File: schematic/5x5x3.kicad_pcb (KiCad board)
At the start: 4 copper layers, 100 x 100 mm, 137 parts, among them J1 SW Debug, J11 Conn_01x03_Male, J12 Conn_01x03_Male, J3 Conn_01x03_Male, J4 Conn_01x03_Male, J7 Conn_01x03_Male, SW11 SW, SW12 SW, SW13 SW, SW14 SW, SW21 SW, SW22 SW, SW23 SW, SW24 SW, SW25 SW, SW31 SW, SW32 SW, SW33 SW, SW34 SW, SW35 SW, SW41 SW, SW42 SW, SW43 SW, SW44 SW, SW45 SW, SW51 SW, SW52 SW, SW53 SW, SW54 SW, SW55 SW, SW6 ALPS_EC11, U1 nice_nano v2

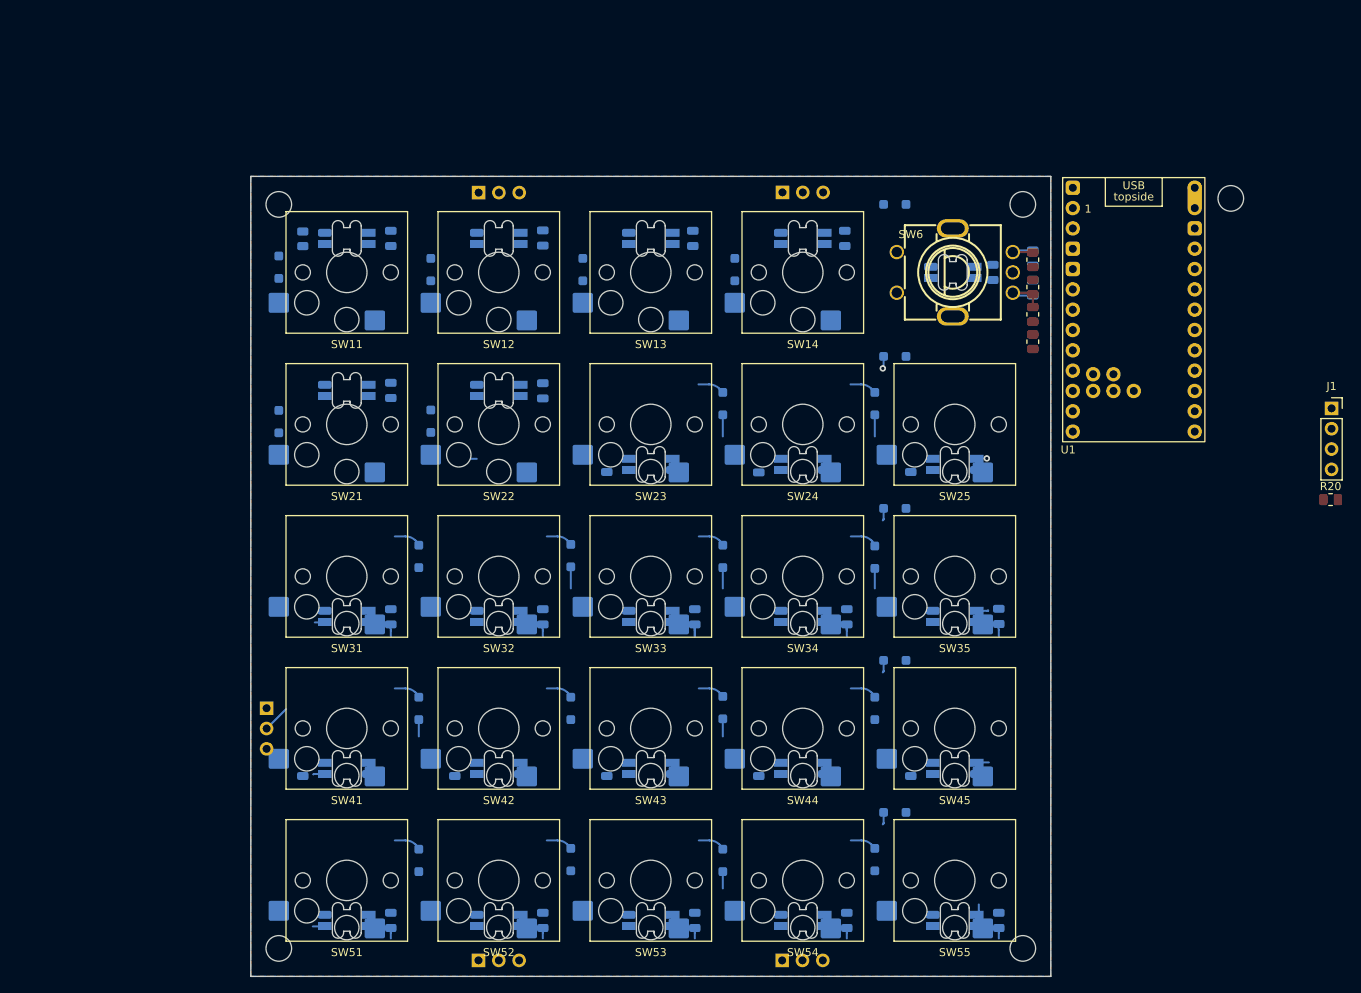
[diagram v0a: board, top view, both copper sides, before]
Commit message: Connect up the keys, rough placing of components
Need to find a good switch, and maybe rearrange the row / col pins to
better align with 5x5 layout.

Currently targetting 4 layer board
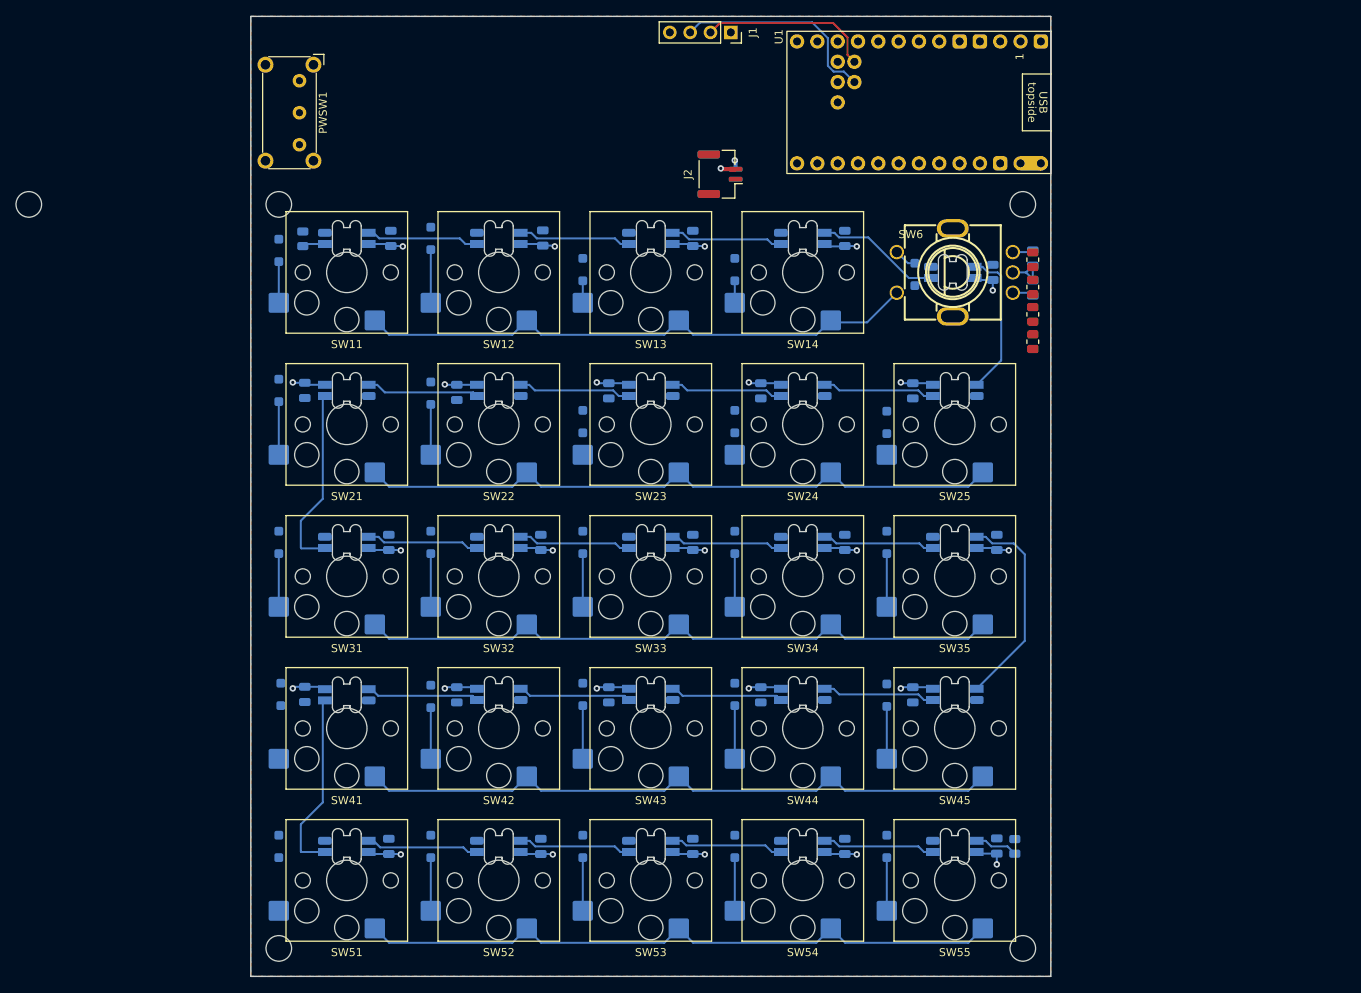
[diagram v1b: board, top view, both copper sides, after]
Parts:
- removed J11, J12, J4, J7: Conn_01x03_Male, Connector_PinSocket_2.54mm:PinSocket_1x03_P2.54mm_Vertical
- removed kibuzzard-62AF6B0E: G***, kibuzzard-62AF6B0E
- removed kibuzzard-62AF6B38: G***, kibuzzard-62AF6B38
- removed kibuzzard-62AF6B7C: G***, kibuzzard-62AF6B7C
- removed kibuzzard-62AF6BA3: G***, kibuzzard-62AF6BA3
- removed kibuzzard-62AF6BAD: G***, kibuzzard-62AF6BAD
- removed kibuzzard-62AF6BF3: G***, kibuzzard-62AF6BF3
- removed kibuzzard-62AF6D1E (x2): G***, kibuzzard-62AF6D1E
- removed kibuzzard-62AF6DB1 (x2): G***, kibuzzard-62AF6DB1
- removed kibuzzard-62AF6E15: G***, kibuzzard-62AF6E15
- removed kibuzzard-62AF6E21: G***, kibuzzard-62AF6E21
- removed kibuzzard-62AF6EB6: G***, kibuzzard-62AF6EB6
- removed kibuzzard-62AF6EDD: G***, kibuzzard-62AF6EDD
- removed kibuzzard-62AF6F00: G***, kibuzzard-62AF6F00
- removed kibuzzard-62AF6F11: G***, kibuzzard-62AF6F11
- added J2: Battery, Connector_JST:JST_GH_BM02B-GHS-TBT_1x02-1MP_P1.25mm_Vertical, F.Cu at (94.7, 37.7)
- added PWSW1: SW_SPST, Button_Switch_THT:SW_E-Switch_EG1224_SPDT_Angled, F.Cu at (42.1, 26.0)
- J3: value Conn_01x03_Male -> Battery; footprint Connector_PinSocket_2.54mm:PinSocket_1x03_P2.54mm_Vertical -> Connector_JST:JST_GH_BM02B-GHS-TBT_1x02-1MP_P1.25mm_Vertical
- R20: moved to B.Cu
- moved ? 150.3 mm to (8.25, 41.5)
- moved J1 88.6 mm to (96.0, 20.0), turned to -90 degrees
- moved R20 58.6 mm to (131.5, 121.8), turned to 90 degrees
- moved U1 39.1 mm to (118.2, 28.8), turned to -90 degrees
- moved J3 30.3 mm to (94.7, 37.7)
- moved D23 17.6 mm to (77.5, 68.7), turned to -90 degrees
- moved D24 17.6 mm to (96.5, 68.7), turned to -90 degrees
- moved D34 17.6 mm to (96.5, 83.8), turned to -90 degrees
- moved D31 17.6 mm to (39.5, 83.8), turned to -90 degrees
- moved D33 17.6 mm to (77.5, 83.8), turned to -90 degrees
- moved D44 17.6 mm to (96.5, 102.8), turned to -90 degrees
- moved D51 17.6 mm to (39.5, 121.8), turned to -90 degrees
- moved D53 17.6 mm to (77.5, 121.8), turned to -90 degrees
- moved D32 17.6 mm to (58.5, 83.8), turned to -90 degrees
- moved D43 17.6 mm to (77.5, 102.8), turned to -90 degrees
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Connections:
- C11 pad 1: Vusb -> Vext
- C12 pad 1: Vusb -> Vext
- C13 pad 1: Vusb -> Vext
- C14 pad 1: Vusb -> Vext
- C15 pad 1: Vusb -> Vext
- C21 pad 1: Vusb -> Vext
- C22 pad 1: Vusb -> Vext
- C23 pad 1: Vusb -> Vext
- C24 pad 1: Vusb -> Vext
- C25 pad 1: Vusb -> Vext
- C31 pad 1: Vusb -> Vext
- C32 pad 1: Vusb -> Vext
- C33 pad 1: Vusb -> Vext
- C34 pad 1: Vusb -> Vext
- C35 pad 1: Vusb -> Vext
- C41 pad 1: Vusb -> Vext
- C42 pad 1: Vusb -> Vext
- C43 pad 1: Vusb -> Vext
- C44 pad 1: Vusb -> Vext
- C45 pad 1: Vusb -> Vext
- C51 pad 1: Vusb -> Vext
- C52 pad 1: Vusb -> Vext
- C53 pad 1: Vusb -> Vext
- C54 pad 1: Vusb -> Vext
- C55 pad 1: Vusb -> Vext
- J1 pad 1: +3V3 -> Vbatt
- J3 pad 1: GND -> Vbatt
- LED11 pad 1: Vusb -> Vext
- LED12 pad 1: Vusb -> Vext
- LED13 pad 1: Vusb -> Vext
- LED14 pad 1: Vusb -> Vext
- LED15 pad 1: Vusb -> Vext
- LED21 pad 1: Vusb -> Vext
- LED22 pad 1: Vusb -> Vext
- LED23 pad 1: Vusb -> Vext
- LED24 pad 1: Vusb -> Vext
- LED25 pad 1: Vusb -> Vext
- LED31 pad 1: Vusb -> Vext
- LED32 pad 1: Vusb -> Vext
- LED33 pad 1: Vusb -> Vext
- LED34 pad 1: Vusb -> Vext
- LED35 pad 1: Vusb -> Vext
- LED41 pad 1: Vusb -> Vext
- LED42 pad 1: Vusb -> Vext
- LED43 pad 1: Vusb -> Vext
- LED44 pad 1: Vusb -> Vext
- LED45 pad 1: Vusb -> Vext
- LED51 pad 1: Vusb -> Vext
- LED52 pad 1: Vusb -> Vext
- LED53 pad 1: Vusb -> Vext
- LED54 pad 1: Vusb -> Vext
- LED55 pad 1: Vusb -> Vext
- R15 pad 2: Net-(C19-Pad1) -> unconnected-(R15-Pad2)
- R16 pad 1: Vusb -> Vbatt
- R17 pad 1: Vusb -> Vbatt
- R19 pad 2: unconnected-(R19-Pad2) -> BACKLIGHTIN
- U1 pad 13: unconnected-(U1-BAT+-Pad13) -> Net-(PWSW1-A)
- U1 pad 14: unconnected-(U1-GND-Pad14) -> GND
- U1 pad 16: unconnected-(U1-3V3-Pad16) -> Vext
- U1 pad 28: unconnected-(U1-GND-Pad28) -> GND
- U1 pad 29: unconnected-(U1-BAT+-Pad29) -> Net-(PWSW1-A)
- U1 pad 3: unconnected-(U1-GND-Pad3) -> GND
- U1 pad 4: unconnected-(U1-GND-Pad4) -> GND
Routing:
- net Vext: track 0.00 -> 103.2 mm, vias 0 -> 25
- net ROW3: track 0.00 -> 82.0 mm
- net ROW2: track 0.00 -> 82.0 mm
- net ROW5: track 0.00 -> 82.0 mm
- net ROW4: track 3.40 -> 82.0 mm
- net Vusb: track 76.9 -> 0.00 mm
- net ROTD: track 0.00 -> 71.4 mm
- net SWCLK: track 0.00 -> 26.2 mm
- net Net-(LED35-DOUT): track 2.86 -> 26.2 mm
- net Net-(LED21-DOUT): track 1.16 -> 23.2 mm
- net SWDIO: track 0.00 -> 21.8 mm
- net Net-(LED41-DOUT): track 2.86 -> 23.2 mm
- net Net-(LED15-DOUT): track 1.16 -> 18.6 mm, vias 1 -> 0
- net Net-(LED14-DOUT): track 0.00 -> 15.6 mm
- net Net-(LED31-DOUT): track 0.00 -> 14.1 mm
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- added copper zone on F.Cu, net Vbatt
- added copper zone on In1.Cu, net Vext
- removed copper zone on F.Cu, net Vusb
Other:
- board size 100 x 100 mm -> 100 x 120 mm

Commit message: Adjusted powerswitch, battery terminal, rotary encoder
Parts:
- removed J3: Battery, Connector_JST:JST_GH_BM02B-GHS-TBT_1x02-1MP_P1.25mm_Vertical
- added kibuzzard-685E981C: G***, kibuzzard-685E981C, B.Cu at (120.2, 32.0)
- added kibuzzard-685E9829: G***, kibuzzard-685E9829, B.Cu at (120.2, 26.5)
- J2: moved to B.Cu
- PWSW1: footprint Button_Switch_THT:SW_E-Switch_EG1224_SPDT_Angled -> PCM_marbastlib-various:SW_MSK12C02-HB; moved to B.Cu
- moved ? 121.7 mm to (129.2, 28.8), turned to 90 degrees
- moved PWSW1 92.2 mm to (134.2, 29.0), turned to 90 degrees
- moved J1 58.1 mm to (38.0, 23.8), turned to 0 degrees
- moved J2 31.0 mm to (124.3, 29.0)
- moved R15 19.8 mm to (127.2, 40.0), turned to -90 degrees
- moved R18 19.3 mm to (122.0, 40.0), turned to -90 degrees
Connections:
- J2 pad 1: Vbatt -> GND
- J2 pad 2: GND -> Vbatt
- PWSW1 pad 1: Net-(PWSW1-A) -> unconnected-(PWSW1-A-Pad1)
- PWSW1 pad 3: (no net) -> Vpowered
- R15 pad 2: unconnected-(R15-Pad2) -> Net-(C19-Pad1)
- R16 pad 1: Vbatt -> Vpowered
- R17 pad 1: Vbatt -> Vpowered
- U1 pad 13: Net-(PWSW1-A) -> Vpowered
- U1 pad 29: Net-(PWSW1-A) -> Vpowered
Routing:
- net SWCLK: track 26.2 -> 0.00 mm
- net SWDIO: track 21.8 -> 0.00 mm
- net Vpowered: track 0.00 -> 20.3 mm
- net Net-(C20-Pad1): track 2.65 -> 21.7 mm
- net Vbatt: track 1.14 -> 14.6 mm, vias 1 -> 0
- net Net-(C19-Pad1): track 2.59 -> 13.3 mm
- net GND: track 7.95 -> 6.05 mm, vias 1 -> 0
- added copper zone on F.Cu, net Vext
- removed copper zone on F.Cu, net Vbatt

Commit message: Routed rows and columns
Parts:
- moved D15 6.75 mm to (117.0, 43.8), turned to -90 degrees
- moved R15 5.25 mm to (122.0, 39.9)
- moved D41 4.16 mm to (39.4, 106.9), turned to -90 degrees
- moved D52 4.15 mm to (58.4, 125.9)
- moved D31 4.15 mm to (39.5, 87.9)
- moved D32 4.15 mm to (58.5, 87.9)
- moved D33 4.15 mm to (77.5, 87.9)
- moved D35 4.15 mm to (115.5, 87.9)
- moved D43 4.15 mm to (77.5, 106.9)
- moved D44 4.15 mm to (96.5, 106.9)
- moved D51 4.15 mm to (39.5, 125.9)
- moved D53 4.15 mm to (77.5, 125.9)
- moved D54 4.15 mm to (96.5, 125.9)
- moved D55 4.15 mm to (115.5, 125.9)
- moved D12 4.15 mm to (58.5, 49.9)
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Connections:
- U1 pad 12: unconnected-(U1-P1.06-LF-Pad12) -> ROTD
- U1 pad 17: COL1 -> ROTB
- U1 pad 18: COL2 -> ROTA
- U1 pad 19: COL3 -> COL5
- U1 pad 21: COL5 -> COL3
- U1 pad 22: ROTD -> COL2
- U1 pad 23: ROW2 -> COL1
- U1 pad 24: ROW3 -> ROW5
- U1 pad 25: ROTA -> ROW2
- U1 pad 26: ROTB -> ROW3
- U1 pad 27: unconnected-(U1-P1.07-LF-Pad27) -> ROW4
- U1 pad 8: ROW4 -> unconnected-(U1-P0.24-Pad8)
- U1 pad 9: ROW5 -> unconnected-(U1-P1.00-Pad9)
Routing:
- net COL1: track 0.00 -> 155.9 mm, vias 0 -> 5
- net COL2: track 0.00 -> 139.3 mm, vias 0 -> 5
- net ROW5: track 82.0 -> 219.2 mm, vias 0 -> 1
- net ROW4: track 82.0 -> 208.8 mm, vias 0 -> 1
- net COL3: track 0.00 -> 122.9 mm, vias 0 -> 5
- net ROW3: track 82.0 -> 191.3 mm, vias 0 -> 1
- net COL4: track 0.00 -> 106.4 mm, vias 0 -> 5
- net COL5: track 0.00 -> 96.7 mm, vias 0 -> 5
- net ROW2: track 82.0 -> 173.7 mm, vias 0 -> 1
- net ROTD: track 71.4 -> 140.5 mm, vias 0 -> 1
- net Net-(D12-A): track 6.65 -> 2.50 mm
- net Net-(D55-A): track 6.65 -> 2.50 mm
- net Net-(D54-A): track 6.65 -> 2.50 mm
- net Net-(D53-A): track 6.65 -> 2.50 mm
- net Net-(D44-A): track 6.65 -> 2.50 mm
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
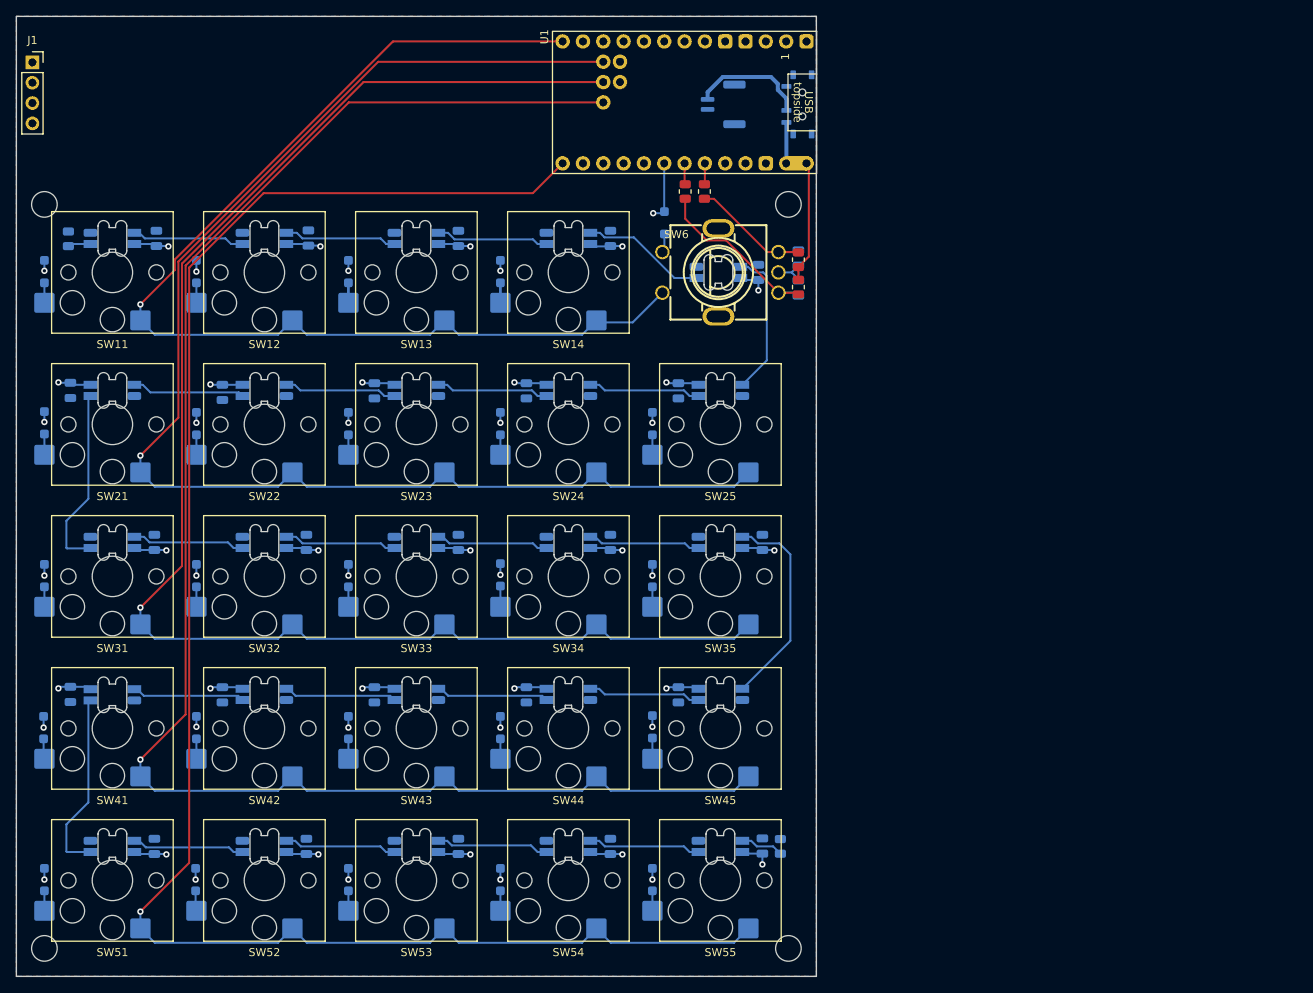
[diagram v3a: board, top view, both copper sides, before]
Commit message: Back to 100x100; aim for 5x5x2 hw compat now
After dithering a long time I am going back to 100x100;

1. 5x5x3 keyboard can then be used on a 5x5x2 carrier, and vice versa.
2. I2C oled screen does not fit nicely in the room I had
3. zmk support for both rgb and i2c powercontrol is in
   development (and has been for some time)
4. With expressive leds, who needs another screen
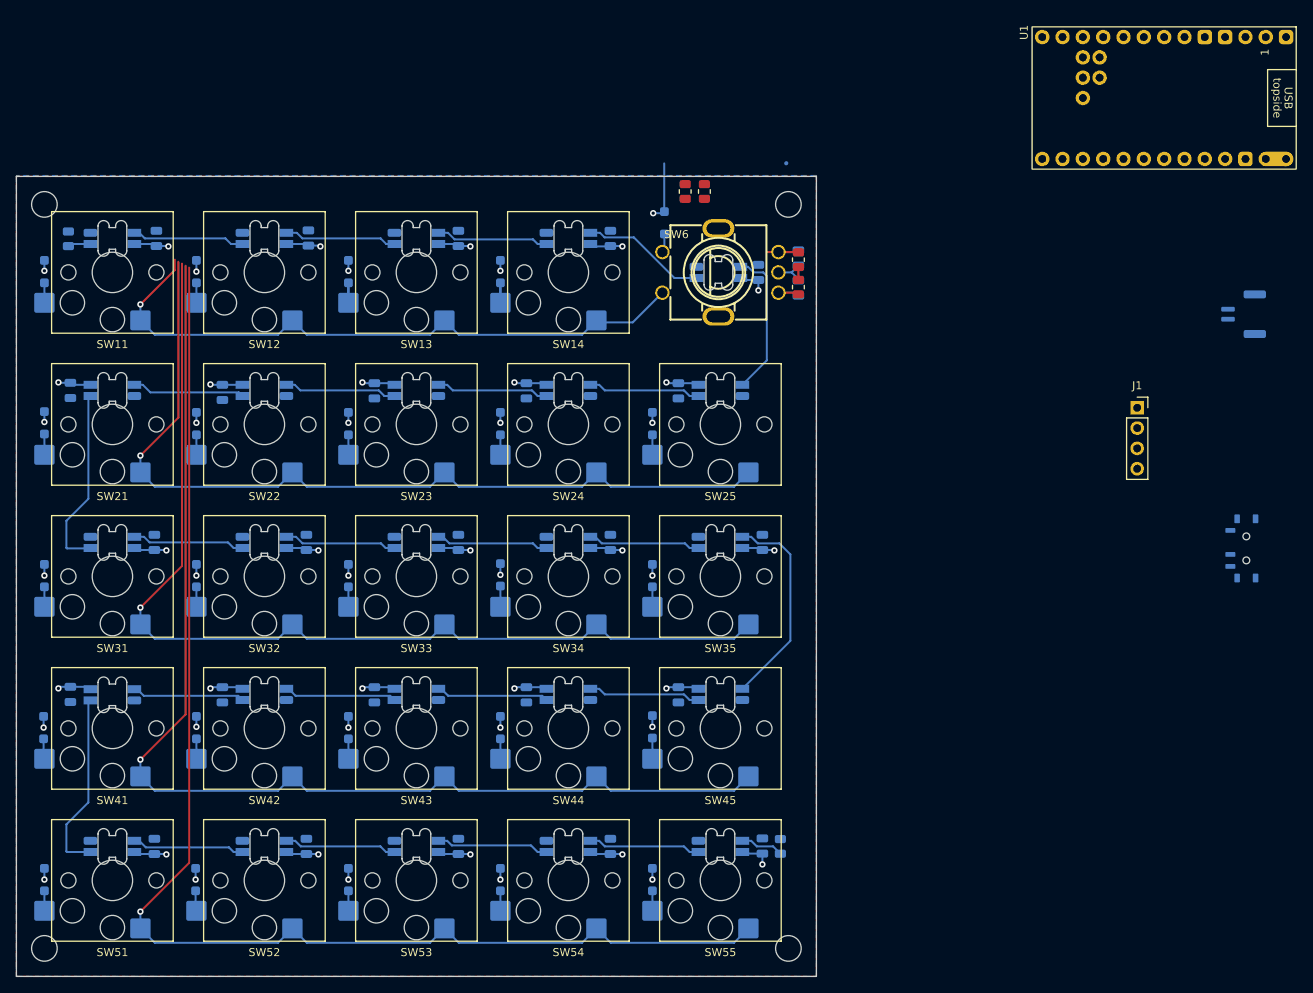
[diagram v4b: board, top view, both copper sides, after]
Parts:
- removed ?: , 
- moved J1 144.7 mm to (176.1, 66.9)
- moved kibuzzard-685E981C 83.1 mm to (169.9, 98.7)
- moved kibuzzard-685E9829 83.1 mm to (169.9, 93.1)
- moved PWSW1 78.5 mm to (189.7, 84.5)
- moved J2 70.1 mm to (189.4, 55.2)
- moved U1 60.0 mm to (178.2, 28.2)
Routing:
- net ROW2: track 173.7 -> 110.3 mm
- net ROW3: track 191.3 -> 129.2 mm
- net ROW4: track 208.8 -> 148.2 mm
- net ROTD: track 140.5 -> 80.7 mm
- net ROW5: track 219.2 -> 167.1 mm
- net Vpowered: track 20.3 -> 1.64 mm
- net Net-(C20-Pad1): track 23.2 -> 5.24 mm
- net Vbatt: track 14.6 -> 0.00 mm
- net Net-(C19-Pad1): track 17.1 -> 6.49 mm
- net ROTB: track 2.63 -> 0.08 mm
- net ROTA: track 2.64 -> 0.11 mm
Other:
- board size 100 x 120 mm -> 100 x 100 mm
